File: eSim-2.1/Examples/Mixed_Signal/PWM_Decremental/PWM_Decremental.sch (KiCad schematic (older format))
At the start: 16 parts, among them U1 plot_v1, U2 pwmdecrement, U3 plot_v1, U4 adc_bridge_1, U5 adc_bridge_1, U6 plot_v1, U7 plot_v1, U8 dac_bridge_1, U9 plot_v1, X1 lm_741

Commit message: Ngveri update
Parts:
- removed U2: pwmdecrement, symbol pwmdecrement
- added U2: dff, symbol dff
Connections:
- net clk: now also U2.1 (data0)
- net at U8.1 (IN1): now also U2.5 (Nout0)
- net at U5.2 (OUT1): now also U2.4 (enable0)
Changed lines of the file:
@@
 EESchema Schematic File Version 2
+LIBS:PWM_Decremental-rescue
 LIBS:power
 LIBS:switches
@@
 LIBS:eSim_Plot
 LIBS:eSim_Nghdl
+LIBS:eSim_Ngveri
 LIBS:PWM_Decremental-cache
 EELAYER 25 0
@@
 $EndComp
 $Comp
-L eSim_GND #PWR3
+L eSim_GND #PWR01
 U 1 1 5DCD9465
 P 3300 5150
-F 0 "#PWR3" H 3300 4900 50  0001 C CNN
+F 0 "#PWR01" H 3300 4900 50  0001 C CNN
 F 1 "eSim_GND" H 3300 5000 50  0000 C CNN
 F 2 "" H 3300 5150 50  0001 C CNN
@@
 $EndComp
 $Comp
-L eSim_GND #PWR2
+L eSim_GND #PWR02
 U 1 1 5DCD9466
 P 2700 3300
-F 0 "#PWR2" H 2700 3050 50  0001 C CNN
+F 0 "#PWR02" H 2700 3050 50  0001 C CNN
 F 1 "eSim_GND" H 2700 3150 50  0000 C CNN
 F 2 "" H 2700 3300 50  0001 C CNN
@@
 $EndComp
 $Comp
-L eSim_GND #PWR1
+L eSim_GND #PWR03
 U 1 1 5DCD9468
 P 1600 3900
-F 0 "#PWR1" H 1600 3650 50  0001 C CNN
+F 0 "#PWR03" H 1600 3650 50  0001 C CNN
 F 1 "eSim_GND" H 1600 3750 50  0000 C CNN
 F 2 "" H 1600 3900 50  0001 C CNN
@@
 $EndComp
 $Comp
-L eSim_GND #PWR4
+L eSim_GND #PWR04
 U 1 1 5DCD946D
 P 4500 3150
-F 0 "#PWR4" H 4500 2900 50  0001 C CNN
+F 0 "#PWR04" H 4500 2900 50  0001 C CNN
 F 1 "eSim_GND" H 4500 3000 50  0000 C CNN
 F 2 "" H 4500 3150 50  0001 C CNN
@@
 clk
 $Comp
-L eSim_GND #PWR5
+L eSim_GND #PWR05
 U 1 1 5DCD9470
 P 6850 5450
-F 0 "#PWR5" H 6850 5200 50  0001 C CNN
+F 0 "#PWR05" H 6850 5200 50  0001 C CNN
 F 1 "eSim_GND" H 6850 5300 50  0000 C CNN
 F 2 "" H 6850 5450 50  0001 C CNN
@@
 Connection ~ 6250 1850
 Wire Wire Line
-	6400 1950 6150 1950
-Wire Wire Line
 	6150 1950 6150 2200
 Wire Notes Line
@@
 Wire Wire Line
 	9300 6400 9300 4500
-$Comp
-L pwmdecrement U2
-U 1 1 61078941
+Wire Wire Line
+	6400 2150 6300 2150
+Wire Wire Line
+	6300 2150 6300 1950
+Wire Wire Line
+	6300 1950 6150 1950
+$Comp
+L dff U2
+U 1 1 6123E15B
 P 4050 3750
 F 0 "U2" H 6900 5550 60  0000 C CNN
-F 1 "pwmdecrement" H 6900 5750 60  0000 C CNN
+F 1 "dff" H 6900 5750 60  0000 C CNN
 F 2 "" H 6900 5700 60  0000 C CNN
 F 3 "" H 6900 5700 60  0000 C CNN

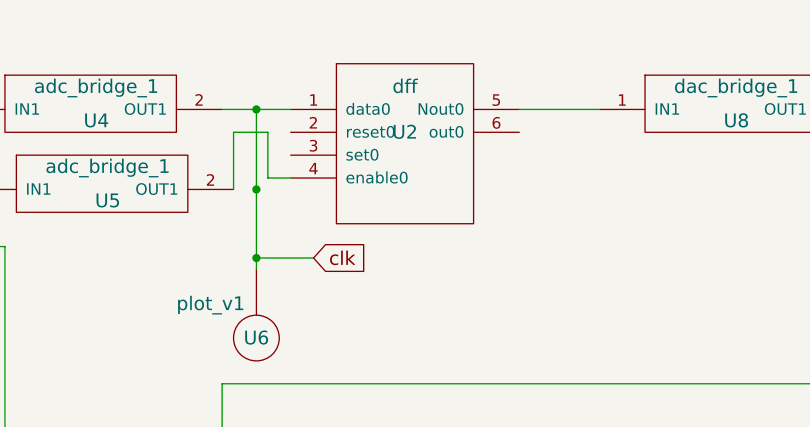
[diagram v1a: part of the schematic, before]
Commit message: Installation Script Changes
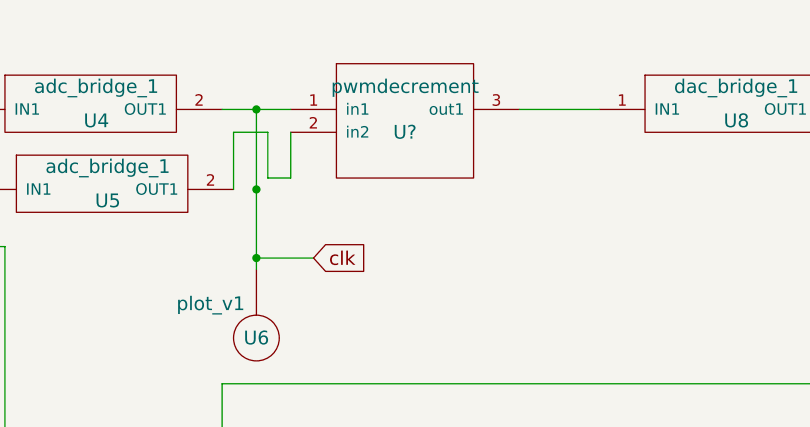
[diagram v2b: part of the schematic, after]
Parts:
- removed U2: dff, symbol dff
- added U?: pwmdecrement, symbol pwmdecrement
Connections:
- net clk: now also U?.1 (in1)
- net at U8.1 (IN1): now also U?.3 (out1)
- net at U5.2 (OUT1): now also U?.2 (in2)
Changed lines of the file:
@@
 	6300 1950 6150 1950
 $Comp
-L dff U2
-U 1 1 6123E15B
+L pwmdecrement U?
+U 1 1 61BDAA39
 P 4050 3750
-F 0 "U2" H 6900 5550 60  0000 C CNN
-F 1 "dff" H 6900 5750 60  0000 C CNN
+F 0 "U?" H 6900 5550 60  0000 C CNN
+F 1 "pwmdecrement" H 6900 5750 60  0000 C CNN
 F 2 "" H 6900 5700 60  0000 C CNN
 F 3 "" H 6900 5700 60  0000 C CNN
@@
 	1    0    0    -1
 $EndComp
+Wire Wire Line
+	6400 2150 6400 1950
 $EndSCHEMATC
